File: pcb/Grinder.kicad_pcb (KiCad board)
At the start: 2 copper layers, 48 x 73 mm, 22 parts, among them J1 Conn_01x06, J2 Conn_01x05, J3 Conn_01x04, J4 Conn_02x05_Odd_Even, Q1 IRLZ44N, U1 ADS1232IPW

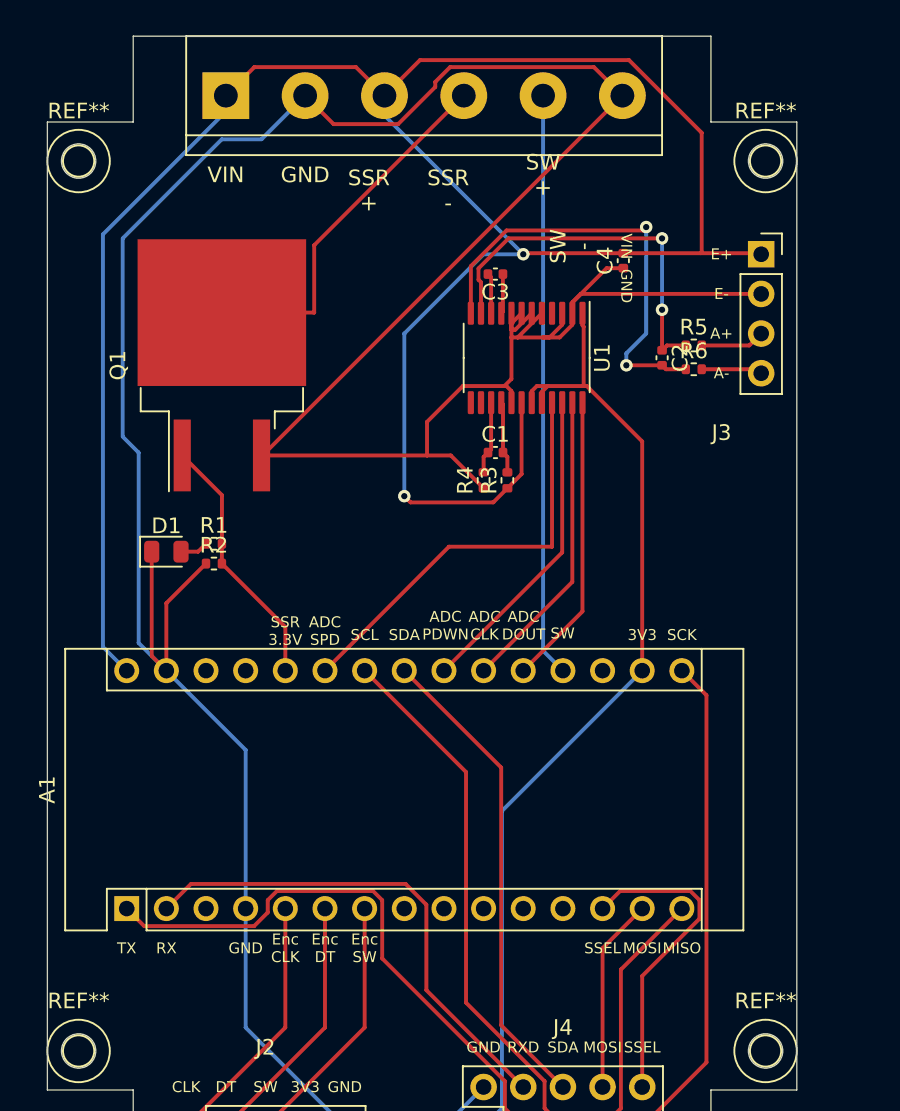
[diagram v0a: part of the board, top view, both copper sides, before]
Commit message: Changed IRLZ44N for 2N7002
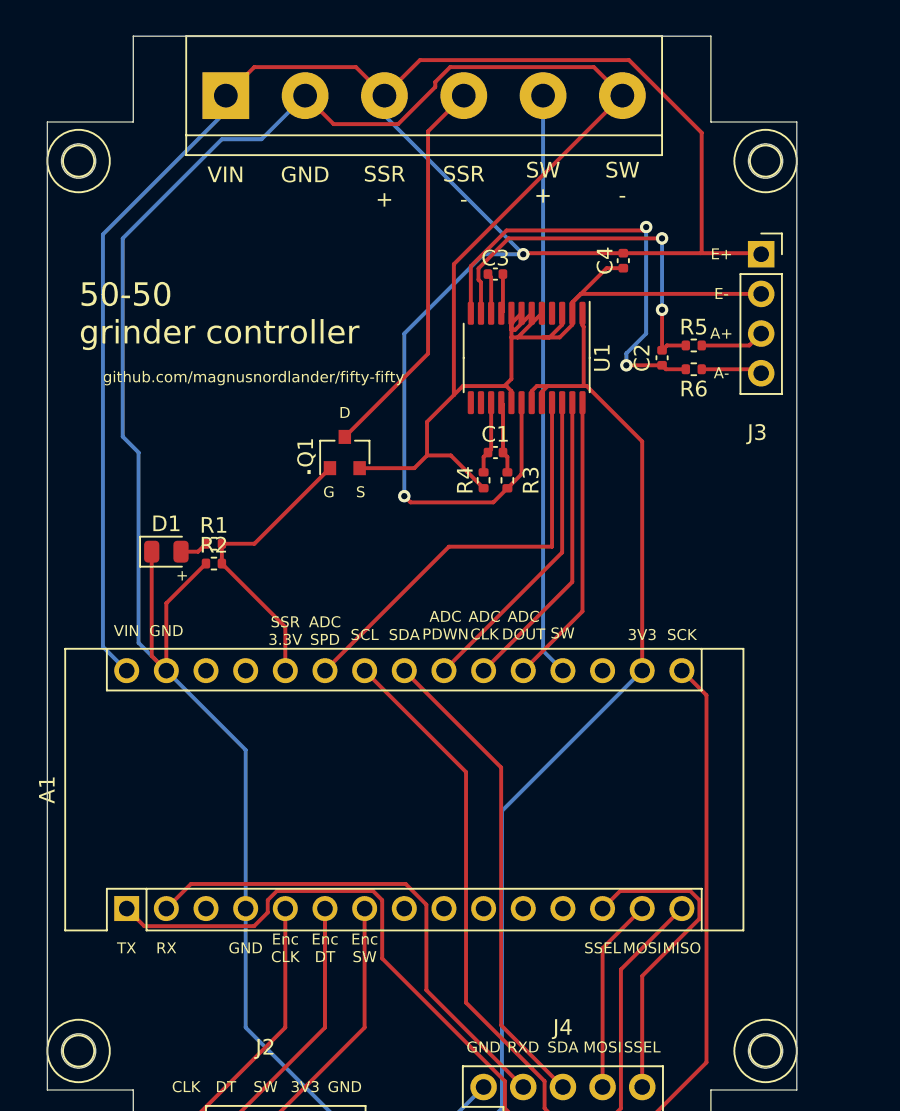
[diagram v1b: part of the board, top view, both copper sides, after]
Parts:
- Q1: value IRLZ44N -> 2N7002; footprint Package_TO_SOT_SMD:TO-263-2 -> Package_TO_SOT_SMD:SOT-23
- moved Q1 9.66 mm to (146.1, 71.1)
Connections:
- Q1 pad 2: SSR_DRAIN -> GND
- Q1 pad 3: GND -> SSR_DRAIN
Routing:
- net GND: track 219.3 -> 204.4 mm
- net SSR_GATE: track 16.5 -> 18.8 mm
- net SSR_DRAIN: track 23.8 -> 25.0 mm
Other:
- board text added: "+"
- board text added: "50-50 grinder controller"
- board text added: "D"
- board text added: "G"
- board text added: "S"
- board text added: "github.com/magnusnordlander/fifty-fifty"
- board text added: "·"
